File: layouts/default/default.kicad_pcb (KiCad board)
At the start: 2 copper layers, 11 parts

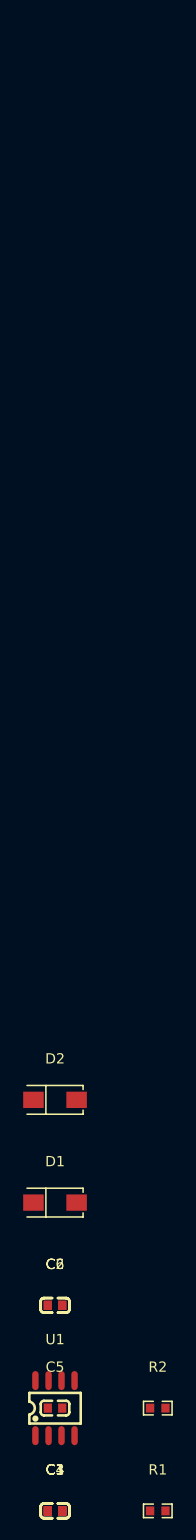
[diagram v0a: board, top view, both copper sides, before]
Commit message: gain stage implemented
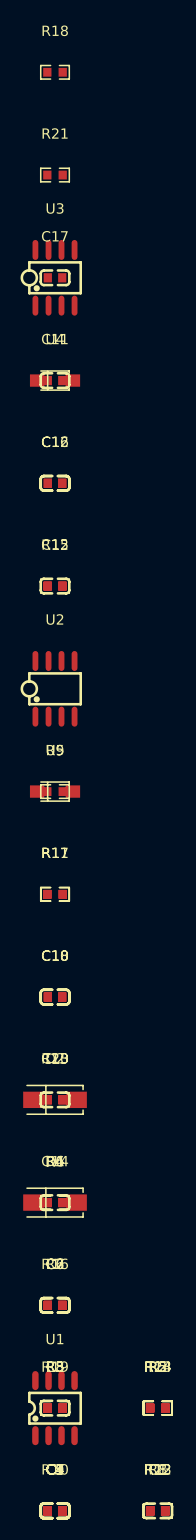
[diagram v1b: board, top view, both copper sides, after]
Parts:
- added C10, C18: 100nF ±10% 50V X7R, atopile:C0603-bd72f6, F.Cu at (0.00, -50.0)
- added C11: 100nF ±10% 50V X7R, atopile:C0603-bd72f6, F.Cu at (0.00, -110.0)
- added C12, C16: 100nF ±10% 50V X7R, atopile:C0603-bd72f6, F.Cu at (0.00, -100.0)
- added C13: 100nF ±10% 50V X7R, atopile:C0603-bd72f6, F.Cu at (0.00, -40.0)
- added C14: 100nF ±10% 50V X7R, atopile:C0603-bd72f6, F.Cu at (0.00, -30.0)
- added C15: 100nF ±10% 50V X7R, atopile:C0603-bd72f6, F.Cu at (0.00, -90.0)
- added C17: 100nF ±10% 50V X7R, atopile:C0603-bd72f6, F.Cu at (0.00, -120.0)
- added C7, C9: 100nF ±10% 50V X7R, atopile:C0603-bd72f6, F.Cu at (0.00, 0.00)
- added C8: 100nF ±10% 50V X7R, atopile:C0603-bd72f6, F.Cu at (10.0, 0.00)
- added R10: 10kΩ ±1% 100mW, atopile:R0603-ebcab9, F.Cu at (0.00, 0.00)
- added R11, R17: 10kΩ ±1% 100mW, atopile:R0603-ebcab9, F.Cu at (0.00, -60.0)
- added R12: 10kΩ ±1% 100mW, atopile:R0603-ebcab9, F.Cu at (0.00, -90.0)
- added R13, R22: 10kΩ ±1% 100mW, atopile:R0603-ebcab9, F.Cu at (10.0, 0.00)
- added R14, R23, R5: 10kΩ ±1% 100mW, atopile:R0603-ebcab9, F.Cu at (10.0, -10.0)
- added R16, R7: 10kΩ ±1% 100mW, atopile:R0603-ebcab9, F.Cu at (0.00, -20.0)
- added R18: 10kΩ ±1% 100mW, atopile:R0603-ebcab9, F.Cu at (0.00, -140.0)
- added R19, R3, R8: 10kΩ ±1% 100mW, atopile:R0603-ebcab9, F.Cu at (0.00, -10.0)
- added R20: 10kΩ ±1% 100mW, atopile:R0603-ebcab9, F.Cu at (0.00, -40.0)
- added R21: 10kΩ ±1% 100mW, atopile:R0603-ebcab9, F.Cu at (0.00, -130.0)
- added R4, R6: 10kΩ ±1% 100mW, atopile:R0603-ebcab9, F.Cu at (0.00, -30.0)
- added R9: 10kΩ ±1% 100mW, atopile:R0603-ebcab9, F.Cu at (0.00, -70.0)
- added U2: , atopile:SOIC-8_L5.0-W4.0-P1.27-LS6.0-BL-294f77, F.Cu at (0.00, -80.0)
- added U3: , atopile:SOIC-8_L5.0-W4.0-P1.27-LS6.0-BL-294f77, F.Cu at (0.00, -120.0)
- added U4: , atopile:SOD-123FL_L2.7-W1.8-LS3.8-RD-0c8348, F.Cu at (0.00, -110.0)
- added U5: , atopile:SOD-123FL_L2.7-W1.8-LS3.8-RD-0c8348, F.Cu at (0.00, -70.0)
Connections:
- C1 pad 1: cathode-1 -> hv
- C2 pad 1: hv -> resistors_ifs[1]
- C5 pad 2: cathode -> cathode-1
- D1 pad 1: cathode -> cathode-1
- D1 pad 2: cathode-1 -> hv
- D2 pad 2: cathode -> cathode-1
- R1 pad 1: line -> resistors_ifs[1]
- R1 pad 2: res_divider-gnd -> gnd
- R2 pad 1: res_divider-hv -> hv
- R2 pad 2: line -> resistors_ifs[1]
- U1 pad 1: cathode-1 -> hv
- U1 pad 8: cathode-1 -> hv

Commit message: summing stage and bug fix
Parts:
- added C19: 100nF ±10% 50V X7R, atopile:C0603-bd72f6, F.Cu at (0.00, -10.0)
- added R15: 10kΩ ±1% 100mW, atopile:R0603-ebcab9, F.Cu at (0.00, 0.00)
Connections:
- C11 pad 2: net-1 -> net-6
- C12 pad 2: net -> net-4
- C13 pad 1: net-4 -> net-5
- C17 pad 2: cathode -> net-1
- C18 pad 1: anode -> cathode-1
- C18 pad 2: net -> net-4
- C2 pad 1: resistors_ifs[1] -> P1INplus
- C3 pad 1: VOUT -> gnd-1
- C5 pad 2: cathode-1 -> cathode
- C6 pad 1: cathode-2 -> VCCplus
- C7 pad 1: net-5 -> net
- C7 pad 2: resistors_ifs[1] -> P1INplus
- C9 pad 1: resistors_ifs[1] -> P1INplus
- D1 pad 1: cathode-1 -> cathode
- D2 pad 1: cathode-2 -> VCCplus
- D2 pad 2: cathode-1 -> cathode
- R1 pad 1: resistors_ifs[1] -> P1INplus
- R12 pad 2: net-4 -> net-5
- R14 pad 1: resistors_ifs[1] -> P1INplus
- R17 pad 1: resistors_ifs[1]-1 -> resistors_ifs[1]
- R2 pad 2: resistors_ifs[1] -> P1INplus
- R20 pad 1: cathode -> net-1
- R20 pad 2: anode -> cathode-1
- R21 pad 1: net -> net-4
- R22 pad 2: resistors_ifs[1] -> P1INplus
- R23 pad 1: resistors_ifs[1]-1 -> resistors_ifs[1]
- R23 pad 2: resistors_ifs[1] -> P1INplus
- R3 pad 1: input_dc_bias_r-net-1 -> input_dc_bias_r-net
- R3 pad 2: input_dc_bias_r-net -> input_dc_bias_r-net-1
- R4 pad 2: net-5 -> net
- R8 pad 2: resistors_ifs[1] -> P1INplus
- R9 pad 1: net-1 -> net-6
- R9 pad 2: resistors_ifs[1] -> P1INplus
- U1 pad 5: VOUT -> gnd-1
- U2 pad 1: resistors_ifs[1] -> P1INplus
- U2 pad 3: resistors_ifs[1] -> P1INplus
- U3 pad 4: tone_opamps-gnd -> gnd-1
- U4 pad 2: anode -> cathode-1
- U5 pad 1: cathode -> cathode-1

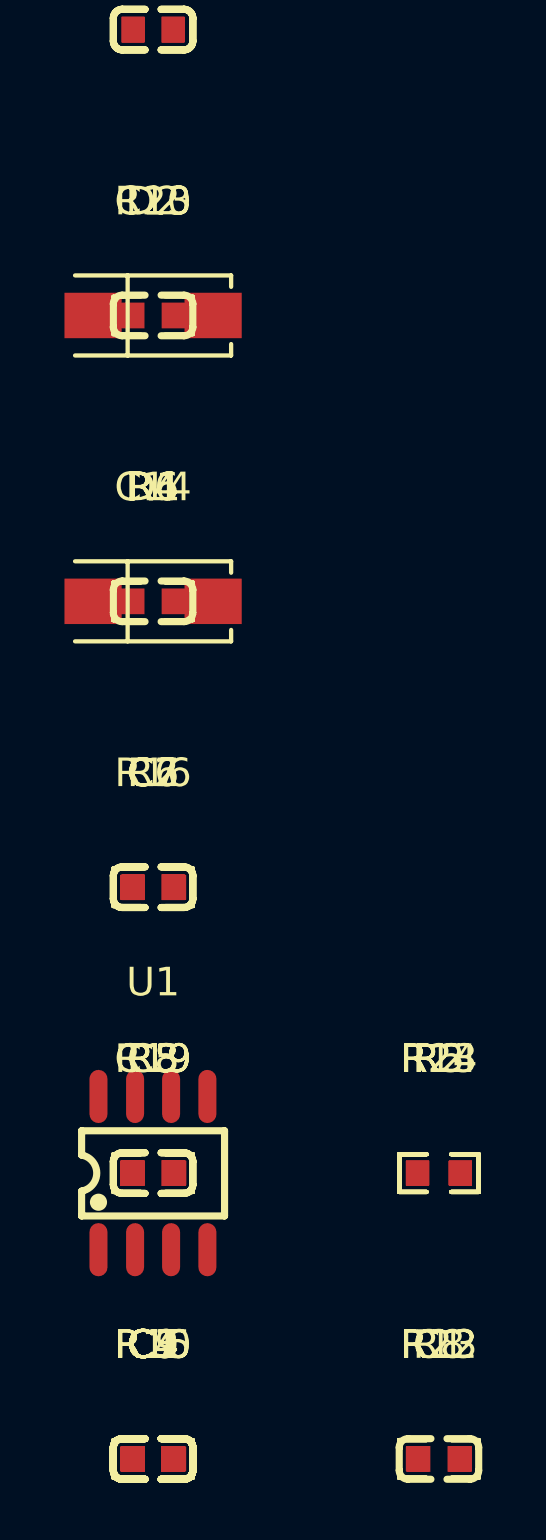
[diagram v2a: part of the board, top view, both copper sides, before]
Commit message: added tone stage
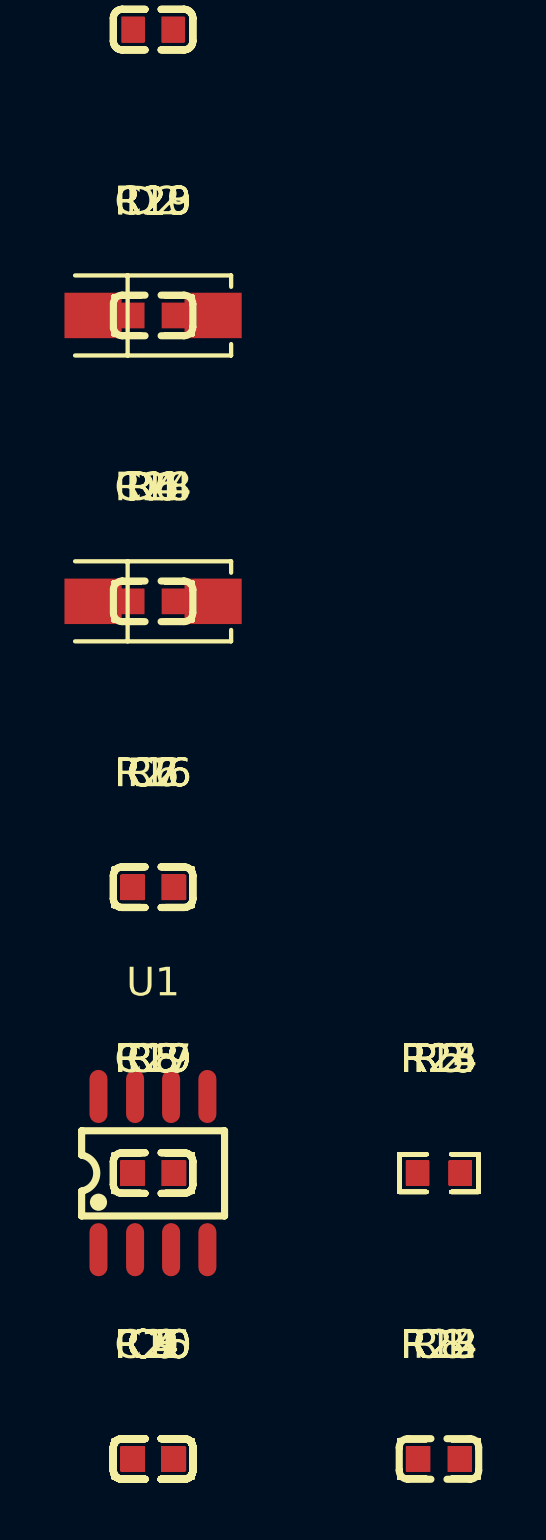
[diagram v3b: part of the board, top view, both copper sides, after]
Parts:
- added C20: 100nF ±10% 50V X7R, atopile:C0603-bd72f6, F.Cu at (0.00, 0.00)
- added R24: 10kΩ ±1% 100mW, atopile:R0603-ebcab9, F.Cu at (10.0, 0.00)
- added R25: 10kΩ ±1% 100mW, atopile:R0603-ebcab9, F.Cu at (10.0, -10.0)
- added R26: 10kΩ ±1% 100mW, atopile:R0603-ebcab9, F.Cu at (0.00, -20.0)
- added R27: 10kΩ ±1% 100mW, atopile:R0603-ebcab9, F.Cu at (0.00, -10.0)
- added R28: 10kΩ ±1% 100mW, atopile:R0603-ebcab9, F.Cu at (0.00, -30.0)
- added R29: 10kΩ ±1% 100mW, atopile:R0603-ebcab9, F.Cu at (0.00, -40.0)
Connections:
- net P2INplus renamed resistors_ifs[0]-1
- net resistors_ifs[0] renamed resistors_ifs[0]-2
- net resistors_ifs[1] renamed resistors_ifs[1]-1
- net wiper renamed wiper-1
- C11 pad 2: net-6 -> net-2
- C12 pad 1: net-3 -> net-5
- C12 pad 2: net-4 -> net-1
- C13 pad 1: net-5 -> net-3
- C15 pad 1: net-2 -> net-6
- C15 pad 2: P2INminus -> P2INminus-1
- C16 pad 1: P2INminus -> P2INminus-1
- C17 pad 2: net-1 -> net
- C18 pad 1: cathode-1 -> cathode
- C18 pad 2: net-4 -> net-1
- C2 pad 1: P1INplus -> non_inverting_input
- C5 pad 2: cathode -> anode
- C7 pad 1: net -> net-4
- C7 pad 2: P1INplus -> non_inverting_input
- C9 pad 1: P1INplus -> non_inverting_input
- D1 pad 1: cathode -> anode
- D2 pad 2: cathode -> anode
- R1 pad 1: P1INplus -> non_inverting_input
- R10 pad 2: net-3 -> net-5
- R12 pad 2: net-5 -> net-3
- R14 pad 1: P1INplus -> non_inverting_input
- R17 pad 2: net-2 -> net-6
- R18 pad 1: net-2 -> net-6
- R18 pad 2: P2INminus -> P2INminus-1
- R19 pad 1: P2INminus -> P2INminus-1
- R2 pad 2: P1INplus -> non_inverting_input
- R20 pad 1: net-1 -> net
- R20 pad 2: cathode-1 -> cathode
- R21 pad 1: net-4 -> net-1
- R22 pad 2: P1INplus -> non_inverting_input
- R23 pad 2: P1INplus -> non_inverting_input
- R3 pad 1: input_dc_bias_r-net -> input_dc_bias_r-net-1
- R3 pad 2: input_dc_bias_r-net-1 -> input_dc_bias_r-net
- R4 pad 2: net -> net-4
- R8 pad 2: P1INplus -> non_inverting_input
- R9 pad 1: net-6 -> net-2
- R9 pad 2: P1INplus -> non_inverting_input
- U2 pad 1: P1INplus -> non_inverting_input
- U2 pad 3: P1INplus -> non_inverting_input
- U2 pad 6: P2INminus -> P2INminus-1
- U3 pad 3: P1INplus -> non_inverting_input
- U3 pad 5: tone_opamps-P2INplus -> non_inverting_input
- U3 pad 6: tone_opamps-P2INminus -> P2INminus
- U3 pad 7: tone_opamps-P2OUT -> P2OUT-1
- U4 pad 2: cathode-1 -> cathode
- U5 pad 1: cathode-1 -> cathode

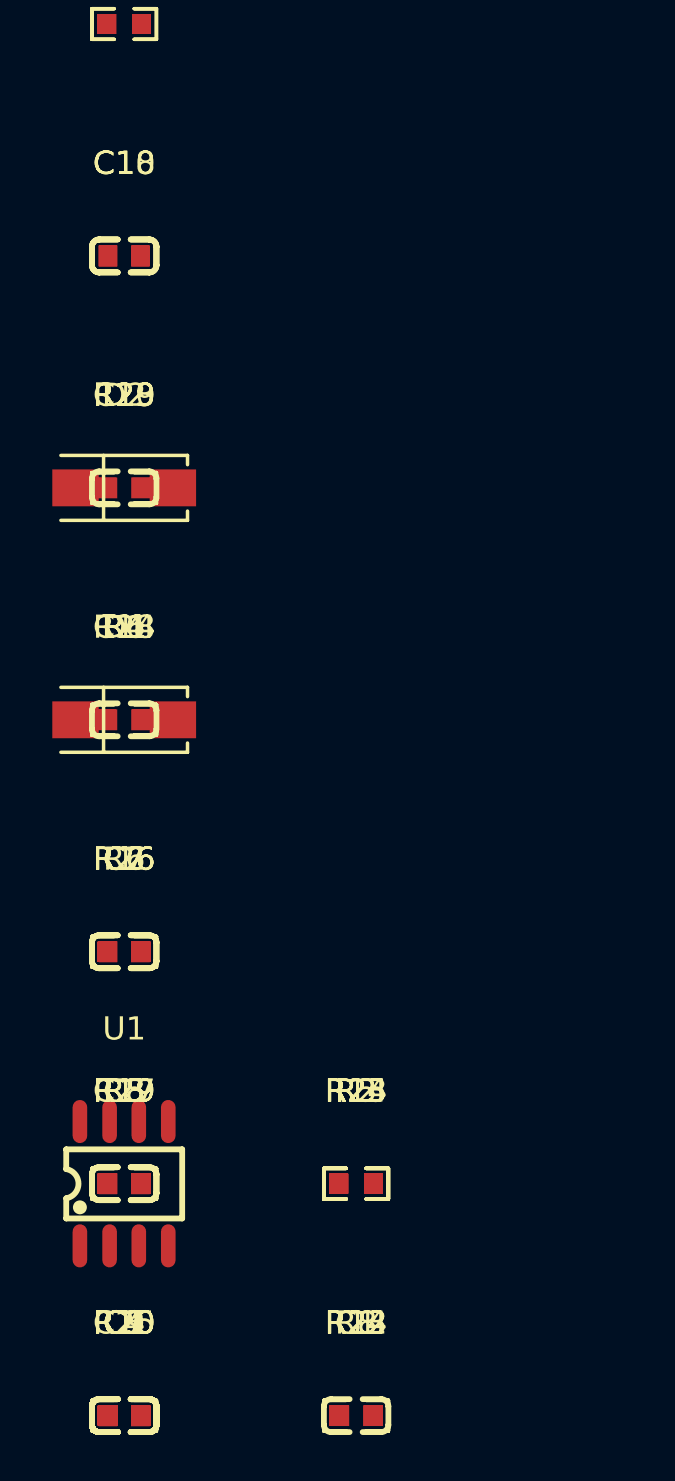
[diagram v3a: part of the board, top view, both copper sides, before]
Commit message: bypass mode added
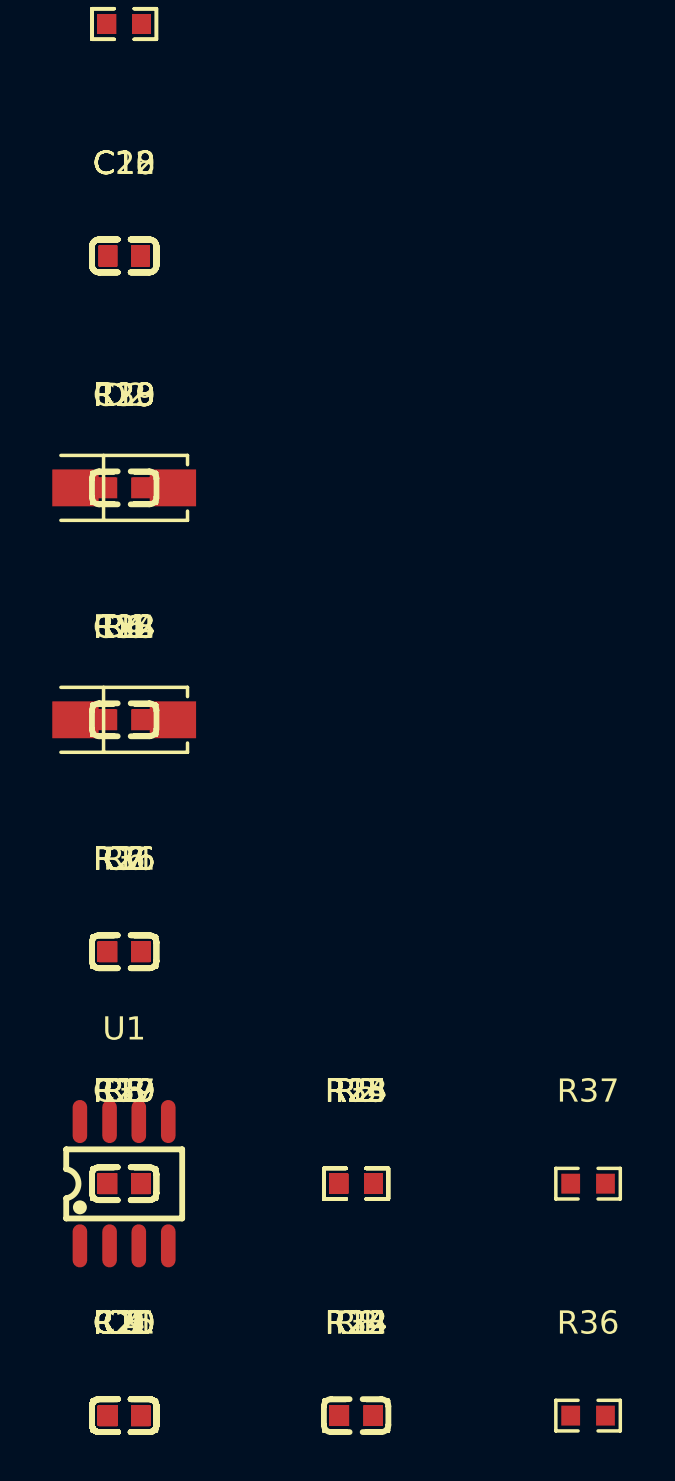
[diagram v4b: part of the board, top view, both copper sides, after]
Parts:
- added C21: 100nF ±10% 50V X7R, atopile:C0603-bd72f6, F.Cu at (0.00, 0.00)
- added C22: 100nF ±10% 50V X7R, atopile:C0603-bd72f6, F.Cu at (0.00, -50.0)
- added R30: 10kΩ ±1% 100mW, atopile:R0603-ebcab9, F.Cu at (0.00, -10.0)
- added R31: 10kΩ ±1% 100mW, atopile:R0603-ebcab9, F.Cu at (0.00, -20.0)
- added R32: 10kΩ ±1% 100mW, atopile:R0603-ebcab9, F.Cu at (0.00, -30.0)
- added R33: 10kΩ ±1% 100mW, atopile:R0603-ebcab9, F.Cu at (0.00, -40.0)
- added R34: 10kΩ ±1% 100mW, atopile:R0603-ebcab9, F.Cu at (10.0, 0.00)
- added R35: 10kΩ ±1% 100mW, atopile:R0603-ebcab9, F.Cu at (10.0, -10.0)
- added R36: 10kΩ ±1% 100mW, atopile:R0603-ebcab9, F.Cu at (20.0, 0.00)
- added R37: 10kΩ ±1% 100mW, atopile:R0603-ebcab9, F.Cu at (20.0, -10.0)
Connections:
- net INPUT renamed INPUT-1
- net anode renamed cathode-1
- net hv renamed hv-1
- C1 pad 2: gnd -> gnd-2
- C10 pad 2: resistors_ifs[0]-2 -> resistors_ifs[0]
- C11 pad 1: resistors_ifs[0]-2 -> resistors_ifs[0]
- C11 pad 2: net-2 -> net-6
- C12 pad 1: net-5 -> net-2
- C12 pad 2: net-1 -> net
- C13 pad 1: net-3 -> net-1
- C15 pad 1: net-6 -> net-5
- C15 pad 2: P2INminus-1 -> P2INminus
- C16 pad 1: P2INminus-1 -> P2INminus
- C17 pad 2: net -> net-7
- C18 pad 2: net-1 -> net
- C2 pad 2: gnd -> gnd-2
- C20 pad 1: wiper -> wiper-1
- C20 pad 2: P2INminus -> P2INminus-1
- C3 pad 1: gnd-1 -> gnd
- C3 pad 2: gnd -> gnd-2
- C6 pad 2: gnd -> gnd-2
- C7 pad 1: net-4 -> net-3
- R1 pad 2: gnd -> gnd-2
- R10 pad 1: wiper-1 -> wiper
- R10 pad 2: net-5 -> net-2
- R11 pad 1: wiper-1 -> wiper
- R12 pad 1: wiper-1 -> wiper
- R12 pad 2: net-3 -> net-1
- R13 pad 1: resistors_ifs[0]-2 -> resistors_ifs[0]
- R13 pad 2: wiper-1 -> wiper
- R14 pad 2: wiper-1 -> wiper
- R17 pad 2: net-6 -> net-5
- R18 pad 1: net-6 -> net-5
- R18 pad 2: P2INminus-1 -> P2INminus
- R19 pad 1: P2INminus-1 -> P2INminus
- R20 pad 1: net -> net-7
- R21 pad 1: net-1 -> net
- R24 pad 1: resistors_ifs[0] -> resistors_ifs[0]-2
- R24 pad 2: wiper -> wiper-1
- R25 pad 2: wiper -> wiper-1
- R27 pad 2: P2INminus -> P2INminus-1
- R28 pad 1: resistors_ifs[0] -> resistors_ifs[0]-2
- R29 pad 1: P2INminus -> P2INminus-1
- R3 pad 1: input_dc_bias_r-net-1 -> input_dc_bias_r-net
- R3 pad 2: input_dc_bias_r-net -> input_dc_bias_r-net-1
- R4 pad 2: net-4 -> net-3
- R7 pad 2: resistors_ifs[0]-2 -> resistors_ifs[0]
- R8 pad 1: resistors_ifs[0]-2 -> resistors_ifs[0]
- R9 pad 1: net-2 -> net-6
- U1 pad 3: gnd -> gnd-2
- U1 pad 5: gnd-1 -> gnd
- U2 pad 4: gnd -> gnd-2
- U2 pad 6: P2INminus-1 -> P2INminus
- U3 pad 4: gnd-1 -> gnd
- U3 pad 6: P2INminus -> P2INminus-1
- U4 pad 1: gnd -> gnd-2
- U5 pad 2: gnd -> gnd-2
